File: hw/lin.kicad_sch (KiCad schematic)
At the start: 12 parts, among them J3 Screw_Terminal_01x03, U5 TJA1029T

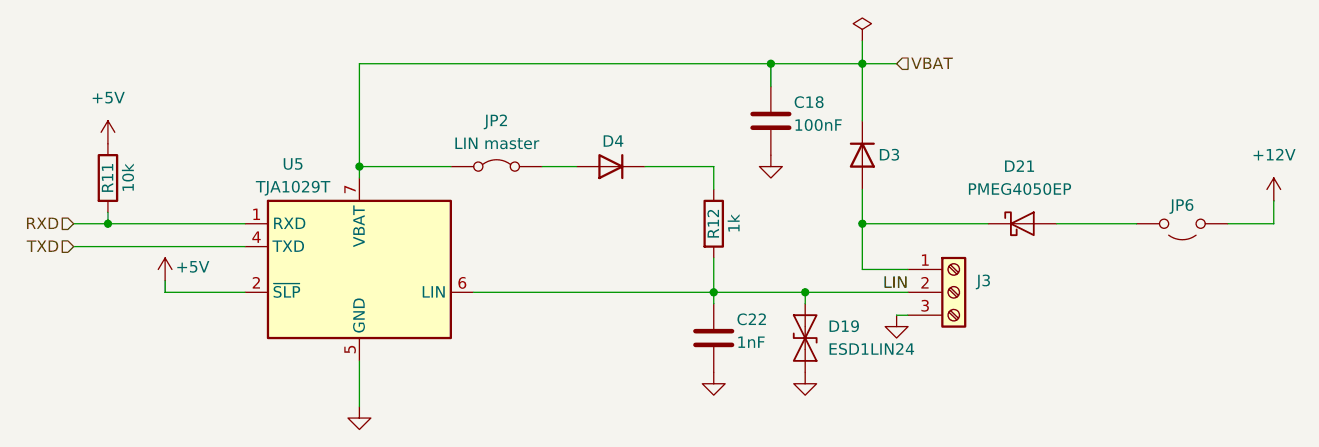
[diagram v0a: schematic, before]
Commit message: hw: manf for jack
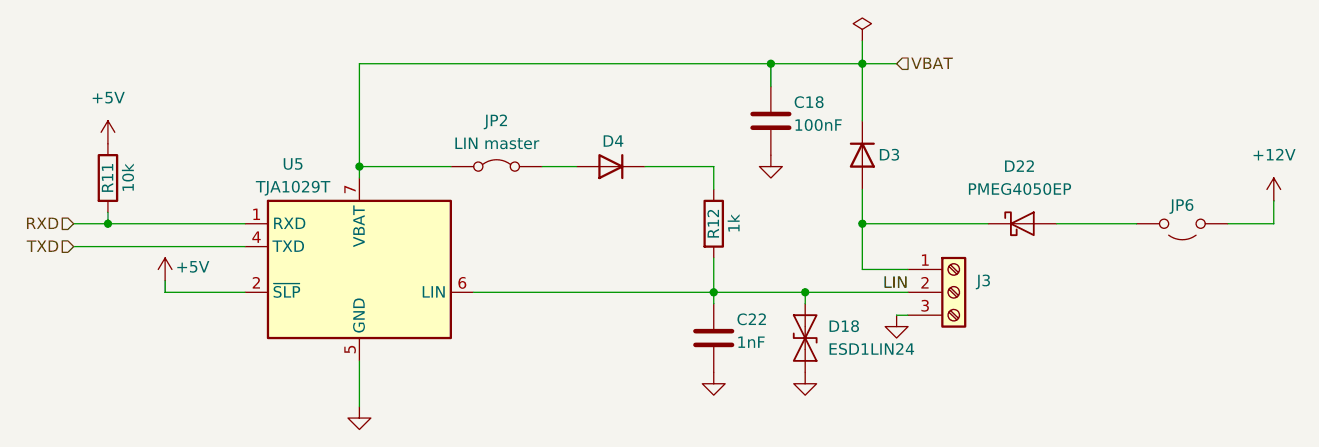
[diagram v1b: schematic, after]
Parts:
- renumbered D19 to D18, D21 to D22
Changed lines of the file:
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@@
 		(dnp no)
 		(fields_autoplaced yes)
-		(property "Reference" "#PWR0120"
+		(property "Reference" "#PWR0121"
 			(at 170.18 116.84 0)
 			(effects
@@
 		(dnp no)
 		(fields_autoplaced yes)
-		(property "Reference" "D21"
+		(property "Reference" "D22"
 			(at 193.9925 87.63 0)
 			(effects
@@
 		(dnp no)
 		(fields_autoplaced yes)
-		(property "Reference" "D19"
+		(property "Reference" "D18"
 			(at 172.72 105.4099 90)
 			(effects

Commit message: hw: manf for LIN connector
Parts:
- J3: manf# (none) -> B3B-XH-A (LF)(SN)
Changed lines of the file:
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@@
+			)
+		)
+		(property "manf#" "B3B-XH-A (LF)(SN)"
+			(at 186.69 101.6 0)
+			(effects
+				(font
+					(size 1.27 1.27)
+				)
+				(hide yes)
 			)
 		)

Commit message: hw: manf for PMEG4050EP,115
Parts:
- D22: manf# (none) -> PMEG4050EP,115
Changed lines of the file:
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@@
+			)
+		)
+		(property "manf#" "PMEG4050EP,115"
+			(at 194.31 93.98 0)
+			(effects
+				(font
+					(size 1.27 1.27)
+				)
+				(hide yes)
 			)
 		)
